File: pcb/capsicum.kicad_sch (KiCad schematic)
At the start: 10 parts, among them Q1 PN2222A, SW2 SW_Push_Dual, SW3 SW_SPDT, U1 ESP32-C3-WROOM-02

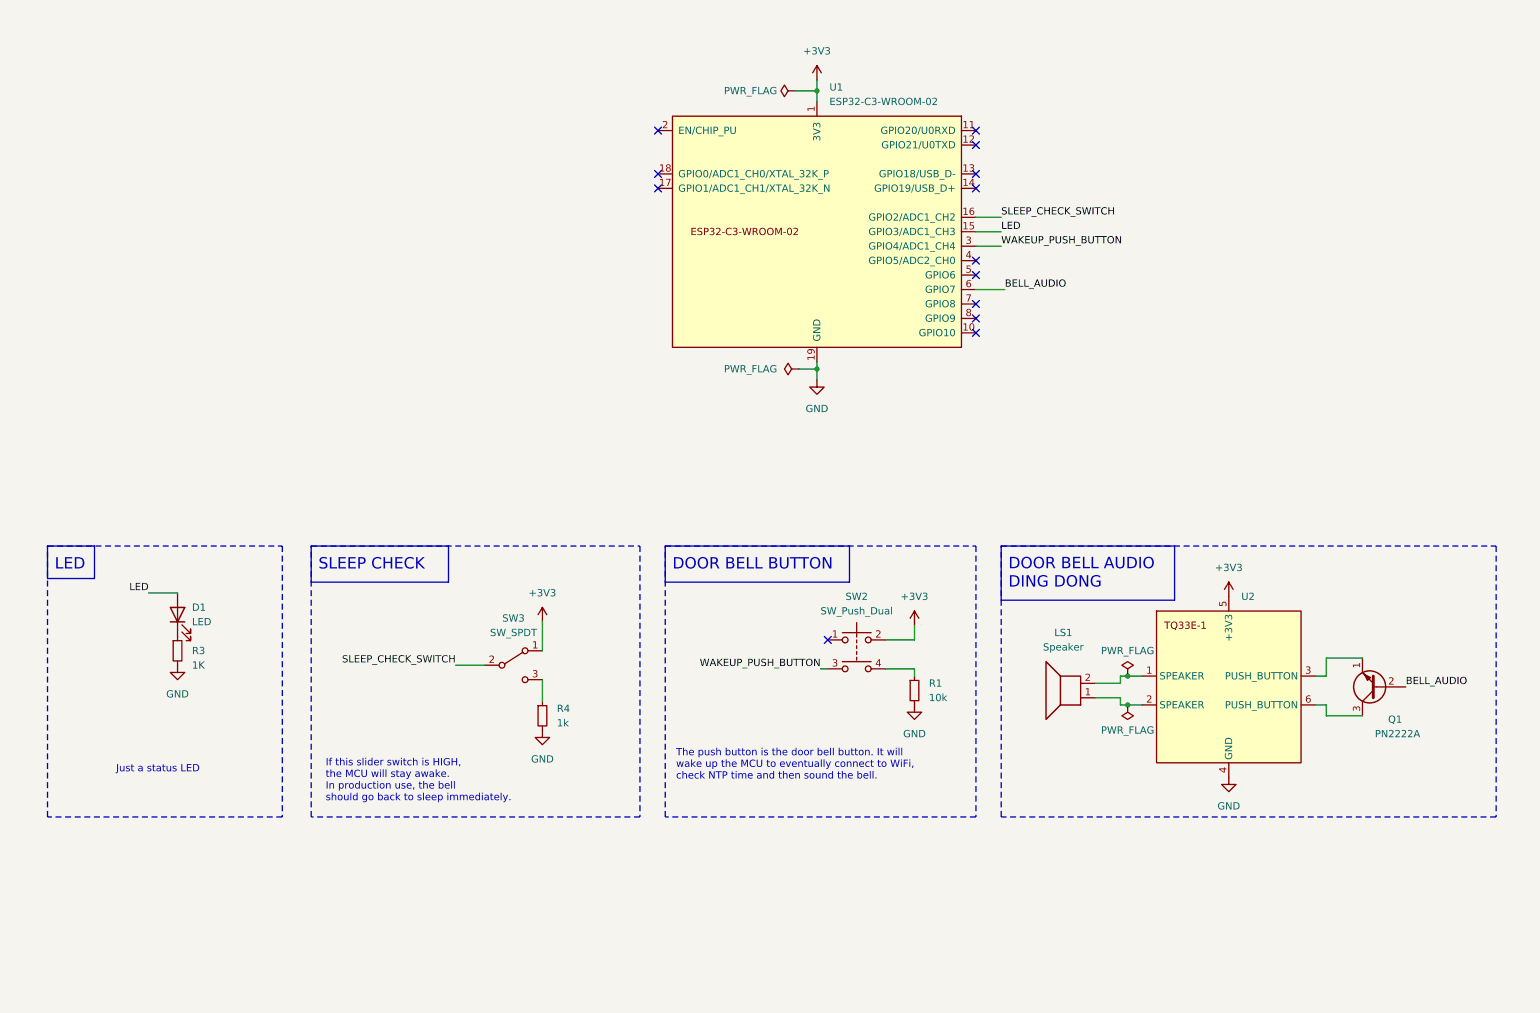
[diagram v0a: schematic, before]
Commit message: feat: add components in the schematic
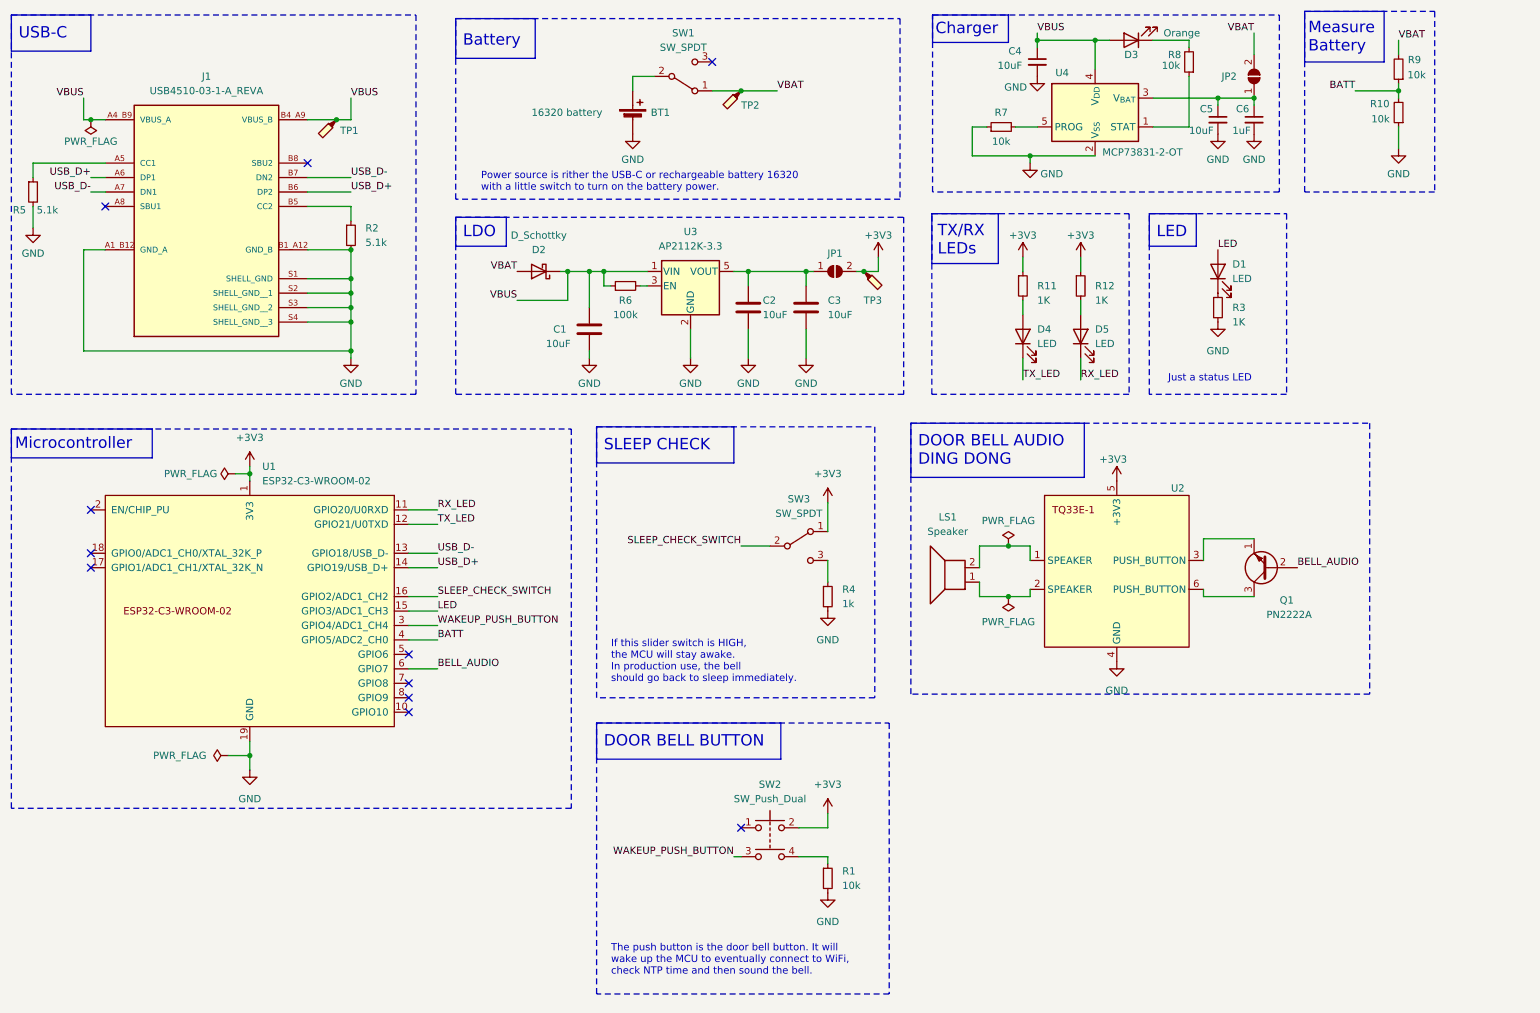
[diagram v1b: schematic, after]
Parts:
- added BT1: 16320 battery, symbol Device:Battery_Cell
- added C1, C2, C3: 10uF, symbol Device:C
- added C4, C5: 10uF, symbol Device:C_Small
- added C6: 1uF, symbol Device:C_Small
- added D2: D_Schottky, symbol Device:D_Schottky
- added D3: Orange, symbol Device:LED
- added D4, D5: LED, symbol Device:LED
- added J1: USB4510-03-1-A_REVA, USB4510-03-1-A_REVA:GCT_USB4510-03-1-A_REVA, symbol GCT_USB_C:USB4510-03-1-A_REVA
- added JP1, JP2: SolderJumper_2_Open, symbol Jumper:SolderJumper_2_Open
- added R10, R7, R8, R9: 10k, symbol Device:R_Small
- added R11, R12: 1K, symbol Device:R_Small
- added R2, R5: 5.1k, symbol Device:R_Small
- added R6: 100k, symbol Device:R_Small
- added SW1: SW_SPDT, symbol Switch:SW_SPDT
- added TP1, TP2, TP3: TestPoint_Probe, symbol Connector:TestPoint_Probe
- added U3: AP2112K-3.3, Package_TO_SOT_SMD:SOT-23-5, symbol Regulator_Linear:AP2112K-3.3
- added U4: MCP73831-2-OT, Package_TO_SOT_SMD:SOT-23-5, symbol Battery_Management:MCP73831-2-OT
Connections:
- net +3V3: now also JP1.2 (B), R11.1, R12.1, TP3.1
- net GND: now also BT1.2 (-), C1.2, C2.2, C3.2, C4.2, C5.2, C6.2, J1.A1_B12 (GND_A), J1.B1_A12 (GND_B), J1.S1 (SHELL_GND), J1.S2 (SHELL_GND__1), J1.S3 (SHELL_GND__2), J1.S4 (SHELL_GND__3), R10.1, R2.2, R5.2, R7.1, U3.2 (GND), U4.2 (V_{SS})
- net RX_LED: now reaches U1.11 (GPIO20/U0RXD)
- net RX_LED: now also D5.1 (K)
- net TX_LED: now reaches U1.12 (GPIO21/U0TXD)
- net TX_LED: now also D4.1 (K)
- net USB_D-: now reaches U1.13 (GPIO18/USB_D-)
- net USB_D-: now also J1.A7 (DN1), J1.B7 (DN2)
- net USB_D+: now reaches U1.14 (GPIO19/USB_D+)
- net USB_D+: now also J1.A6 (DP1), J1.B6 (DP2)
- net BATT: now reaches U1.4 (GPIO5/ADC2_CH0)
- net BATT: now also R10.2, R9.1
- new net: BT1.1 (+), SW1.2 (B)
- new net: R6.2, U3.3 (EN)
- new net: D5.2 (A), R12.2
- new net: D4.2 (A), R11.2
- new net: C5.1, C6.1, JP2.1 (A), U4.3 (V_{BAT})
- new net: J1.A5 (CC1), R5.1
- new net: R7.2, U4.5 (PROG)
- new net: C2.1, C3.1, JP1.1 (A), U3.5 (VOUT)
- new net: R8.1, U4.1 (STAT)
- new net: J1.B5 (CC2), R2.1
- new net: D3.1 (K), R8.2
- new net VBAT: D2.2 (A), JP2.2 (B), R9.2, SW1.1 (A), TP2.1
- new net VBUS: C1.1, C4.1, D2.1 (K), D3.2 (A), J1.A4_B9 (VBUS_A), J1.B4_A9 (VBUS_B), R6.1, TP1.1, U3.1 (VIN), U4.4 (V_{DD})
- no-connect marks 13 -> 11
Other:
- note added: "Battery"
- note added: "Charger"
- note added: "LDO"
- note added: "Measure Battery"
- note added: "Microcontroller"
- note added: "Power source is rither the USB-C or rechargeable battery 16320 with a little switch to turn on the battery power."
- note added: "TX/RX LEDs"
- note added: "USB-C"
- moved on the sheet: D1, LS1, Q1, R1, R3, R4, SW2, SW3, U1, U2

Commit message: feat: add reset button in the schematic
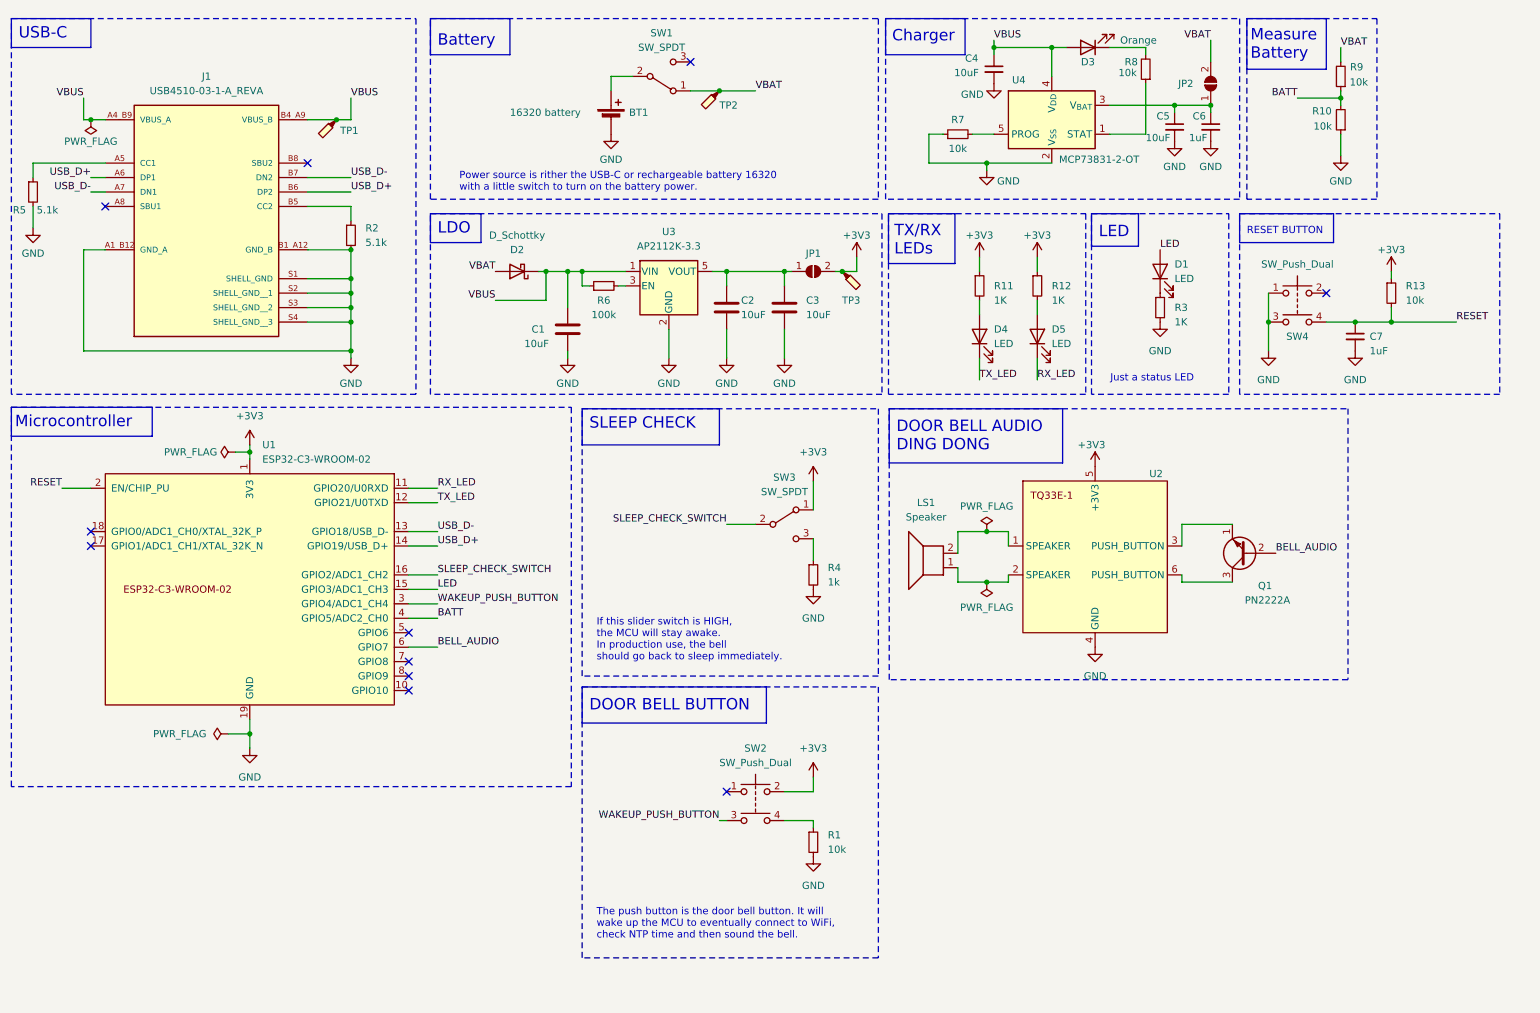
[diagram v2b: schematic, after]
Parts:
- added C7: 1uF, symbol Device:C_Small
- added R13: 10k, symbol Device:R_Small
- added SW4: SW_Push_Dual, symbol Switch:SW_Push_Dual
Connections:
- net +3V3: now also R13.1
- net GND: now also C7.2, SW4.1, SW4.3
- net RESET: now reaches U1.2 (EN/CHIP_PU)
- net RESET: now also C7.1, R13.2, SW4.4
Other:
- note added: "RESET BUTTON"
- moved on the sheet: BT1, C1, C2, C3, C4, C5, C6, D1, D2, D3, D4, D5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

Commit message: feat: add bell connector to the schematic
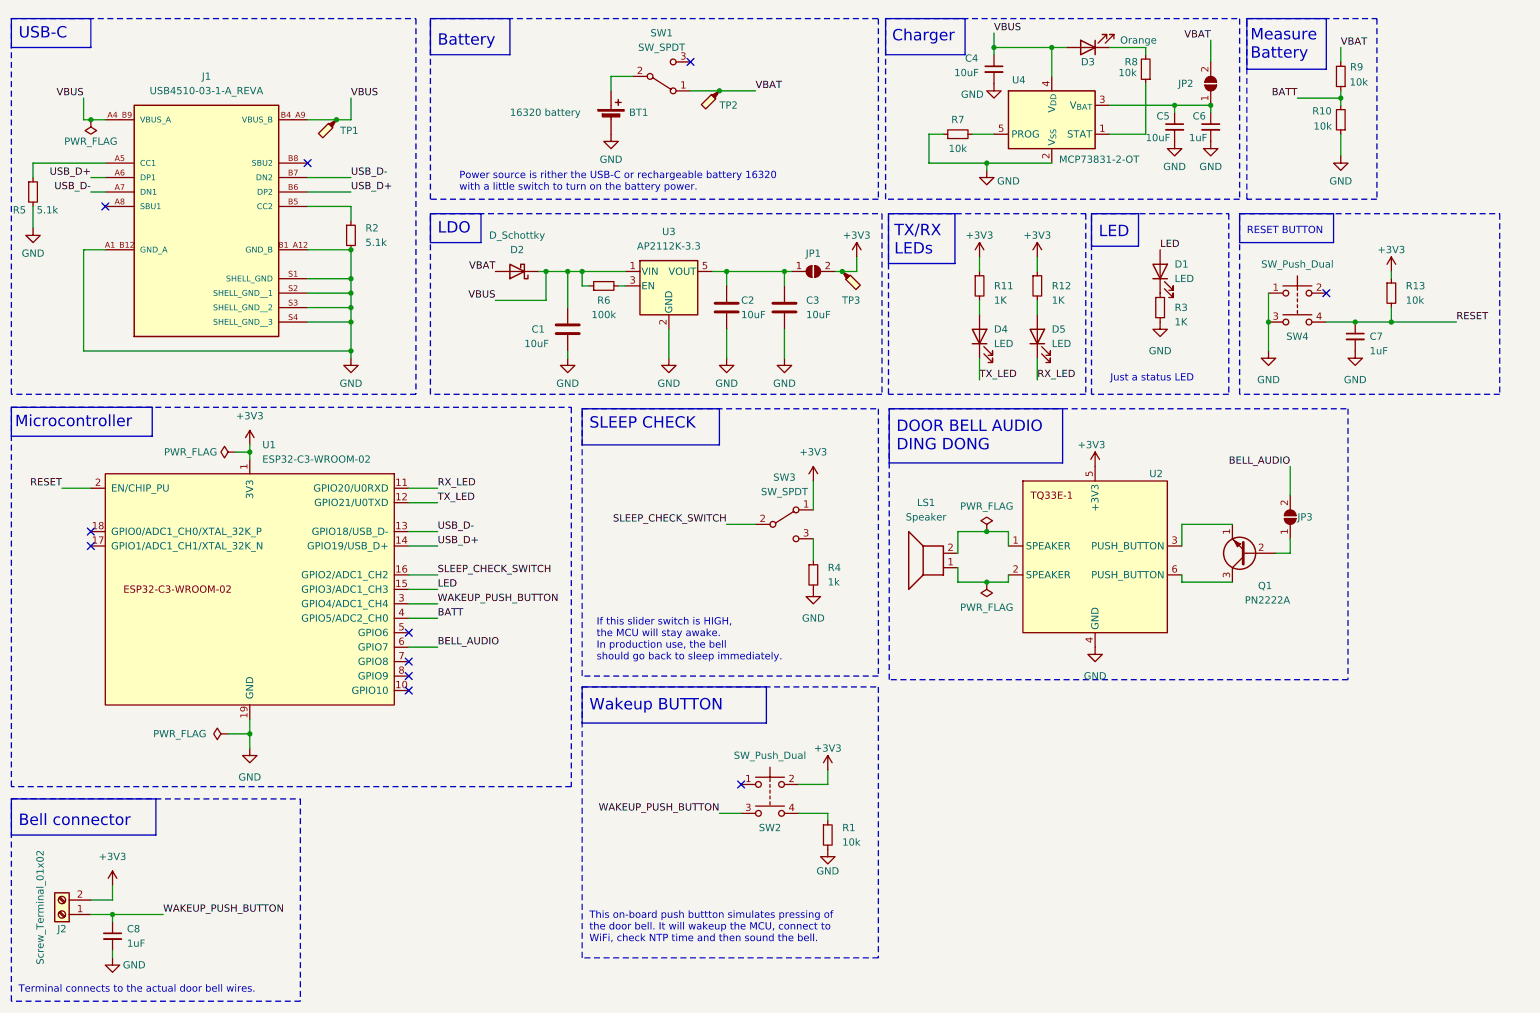
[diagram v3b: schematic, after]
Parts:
- added C8: 1uF, symbol Device:C_Small
- added J2: Screw_Terminal_01x02, symbol Connector:Screw_Terminal_01x02
- added JP3: SolderJumper_2_Open, symbol Jumper:SolderJumper_2_Open
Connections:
- net +3V3: now also J2.2 (Pin_2)
- net BELL_AUDIO: now also JP3.2 (B); no longer Q1.2 (B)
- net GND: now also C8.2
- net WAKEUP_PUSH_BUTTON: now also C8.1, J2.1 (Pin_1)
- new net: JP3.1 (A), Q1.2 (B)
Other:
- note added: "Bell connector"
- note added: "Terminal connects to the actual door bell wires."
- note added: "This on-board push buttton simulates pressing of the door bell. It will wakeup the MCU, connect to WiFi, check NTP time and then sound the bell."
- note added: "Wakeup BUTTON"
- note removed: "DOOR BELL BUTTON"
- note removed: "The push button is the door bell button. It will wake up the MCU to eventually connect to WiFi, check NTP time and then sound the bell."
- moved on the sheet: R1, SW2
